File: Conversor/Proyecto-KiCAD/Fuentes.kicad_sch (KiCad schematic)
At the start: 9 parts, among them J7 ConnAlim12-18, U11 LM7805_TO220, U13 THB3-1211, U14 LM1117-3.3

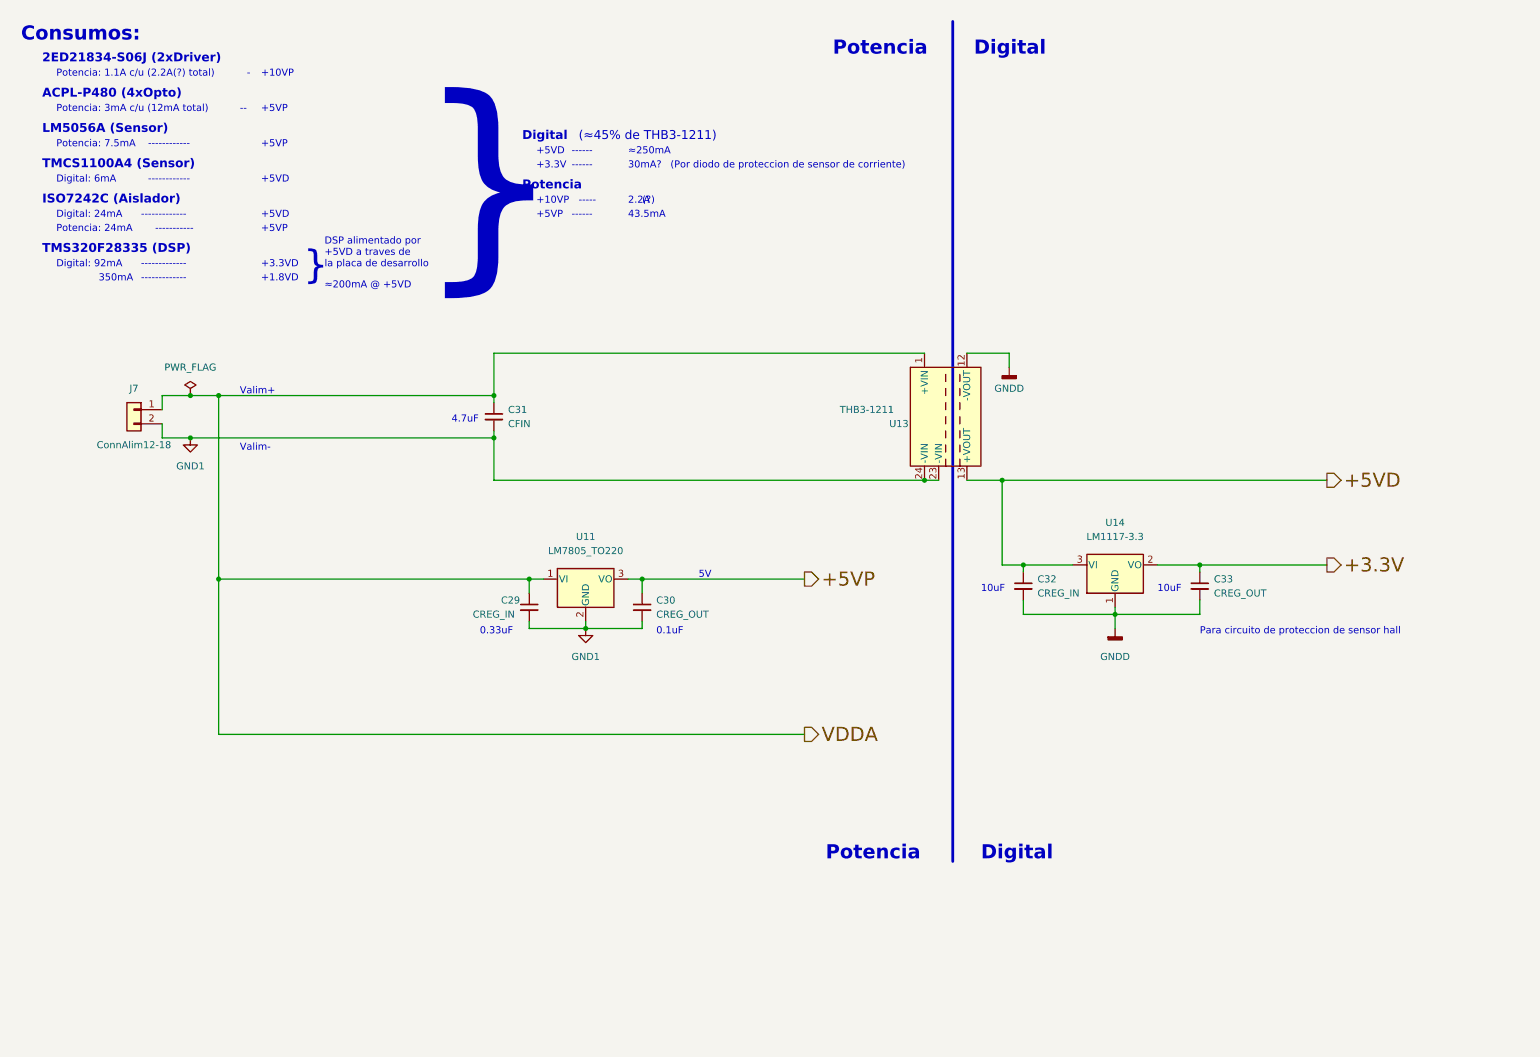
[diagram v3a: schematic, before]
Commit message: Seleccionar componentes de los que me dieron y seguir con la placa adaptadora
- OpAmp OPA365AID para acondicionamiento de señales del sensor de efecto
hall
- Los optos que hay son ACPL-P343 en vez de P480, que necesitan 15-30V
de alimentación. Preguntar si no es mejor cambiarlos por 6N137, de 5V de
Vcc
- Regulador solo hay LM7805 de 5Vout pero también necesito 3.3Vout
- No hay ningún diodo en las cosas que me dieron

Por hacer:
  - Preguntar por los 6N137 y algun regulador de 3V3 out
  - Preguntar por los diodos del puente del conversor
  - Terminar de pasar la placa adaptadora del DSP
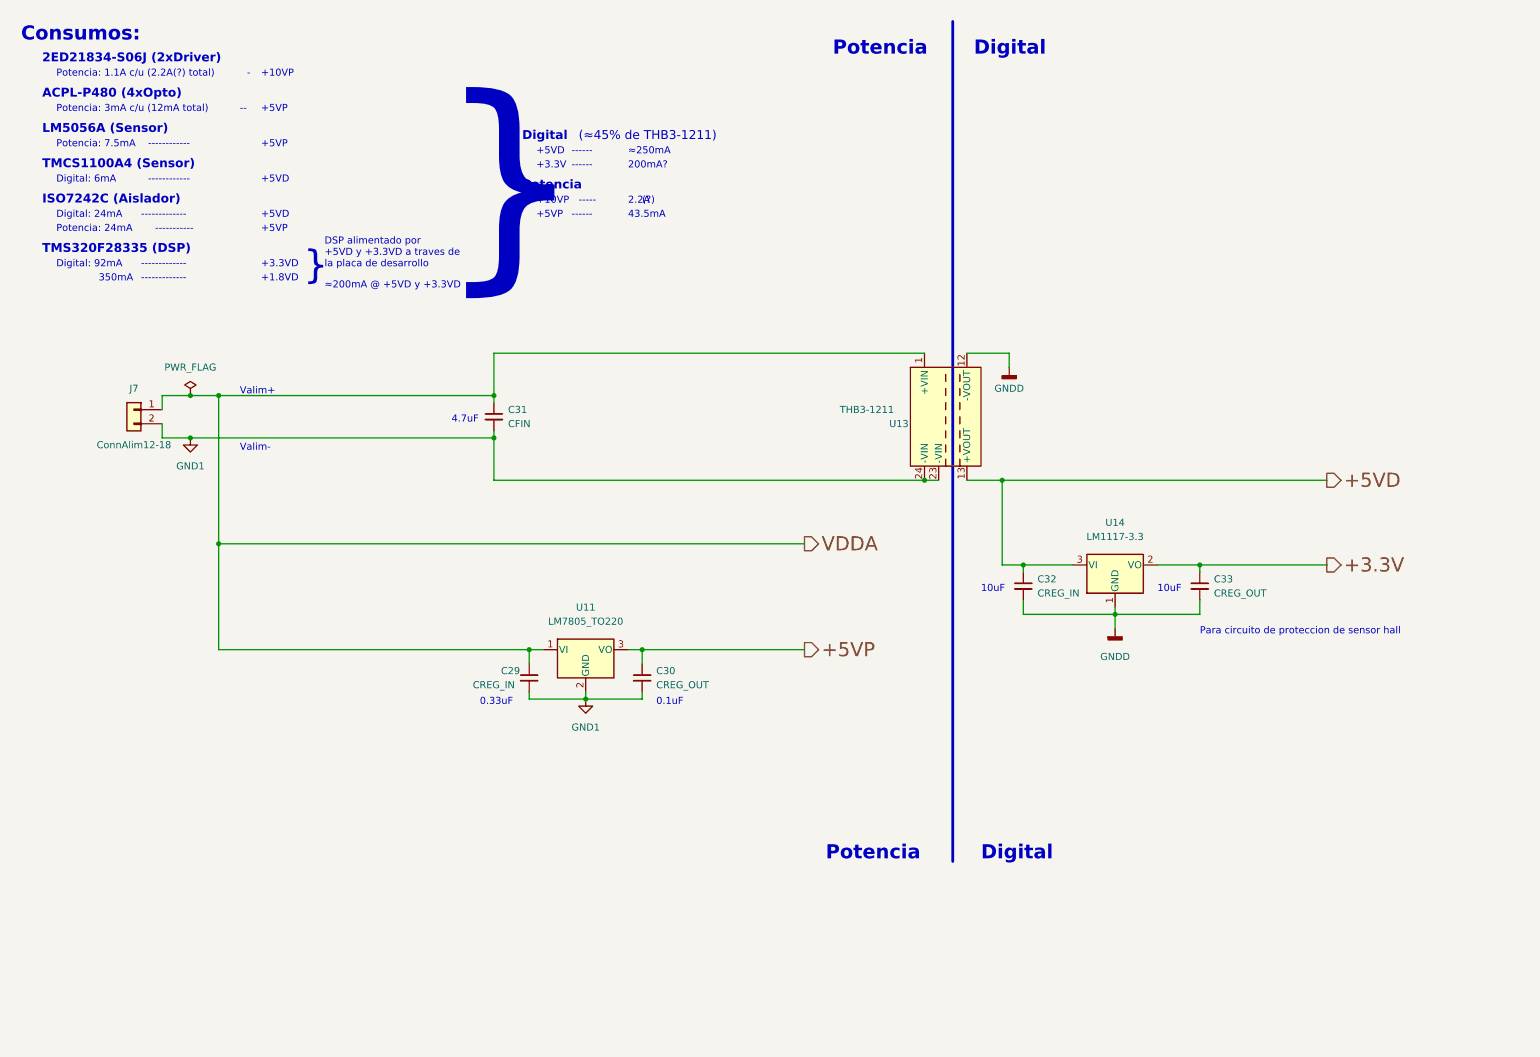
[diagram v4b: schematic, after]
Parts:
- U11: footprint Package_TO_SOT_THT:TO-220-3_Vertical -> Package_TO_SOT_SMD:TO-252-2
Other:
- note added: "200mA?"
- note added: "DSP alimentado por +5VD y +3.3VD a traves de la placa de desarrollo"
- note added: "≈200mA @ +5VD y +3.3VD"
- note removed: "(Por diodo de proteccion de sensor de corriente)"
- note removed: "30mA?"
- note removed: "5V"
- note removed: "DSP alimentado por +5VD a traves de la placa de desarrollo"
- note removed: "≈200mA @ +5VD"
- moved on the sheet: C29, C30, U11

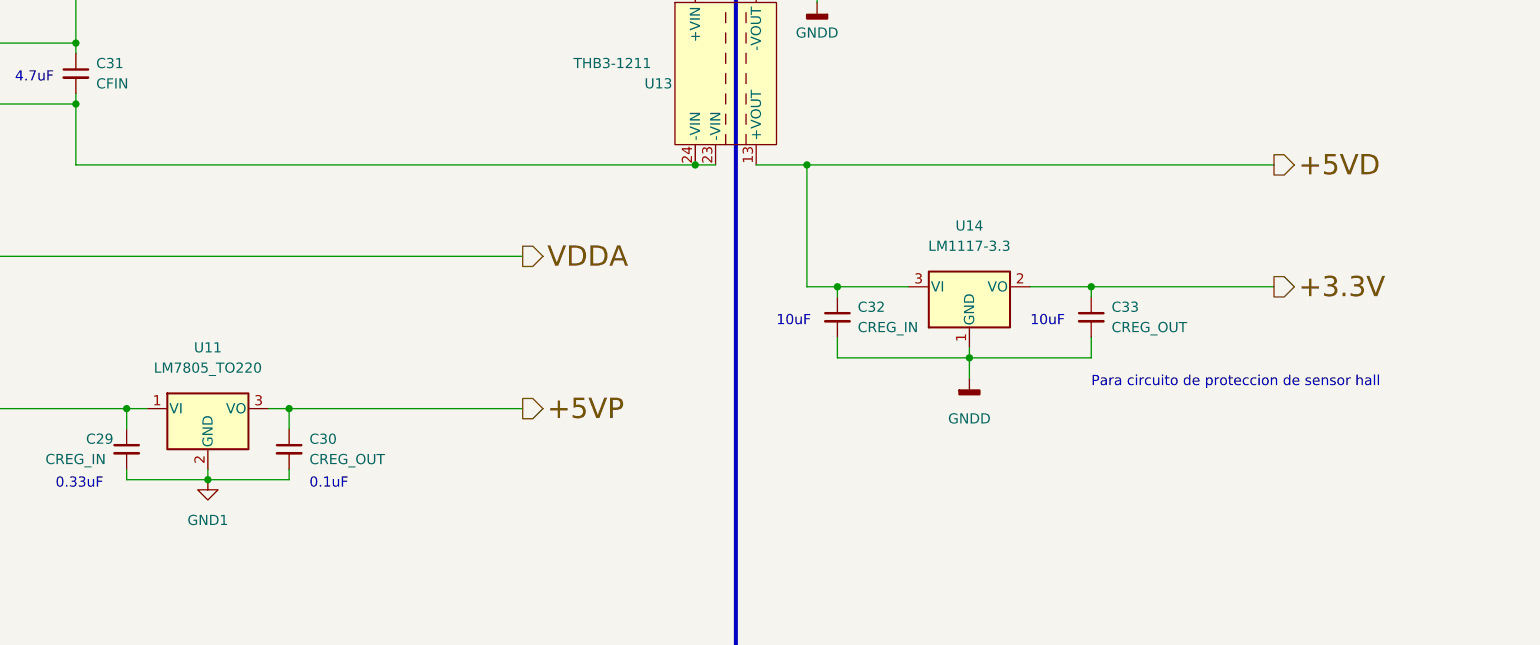
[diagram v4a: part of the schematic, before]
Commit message: Continuar el paso de la placa adaptadora al proyecto
- El bloque de encoder y DAC se eliminan, no son necesarios
- Hay que agregar un selector entre 5V externo y por USB para el DSP, y ver como compatibilizarlo con la alimentación general
- Para el regulador de 3.3V se usa el mismo integrado que en la placa adaptadora (TI LP2985-3.3)
- Los optos son los ACPL-P480 en vez de los P343
Por hacer:
  - Terminar la placa adaptadora (USB-UART, Power Supply e I2C)
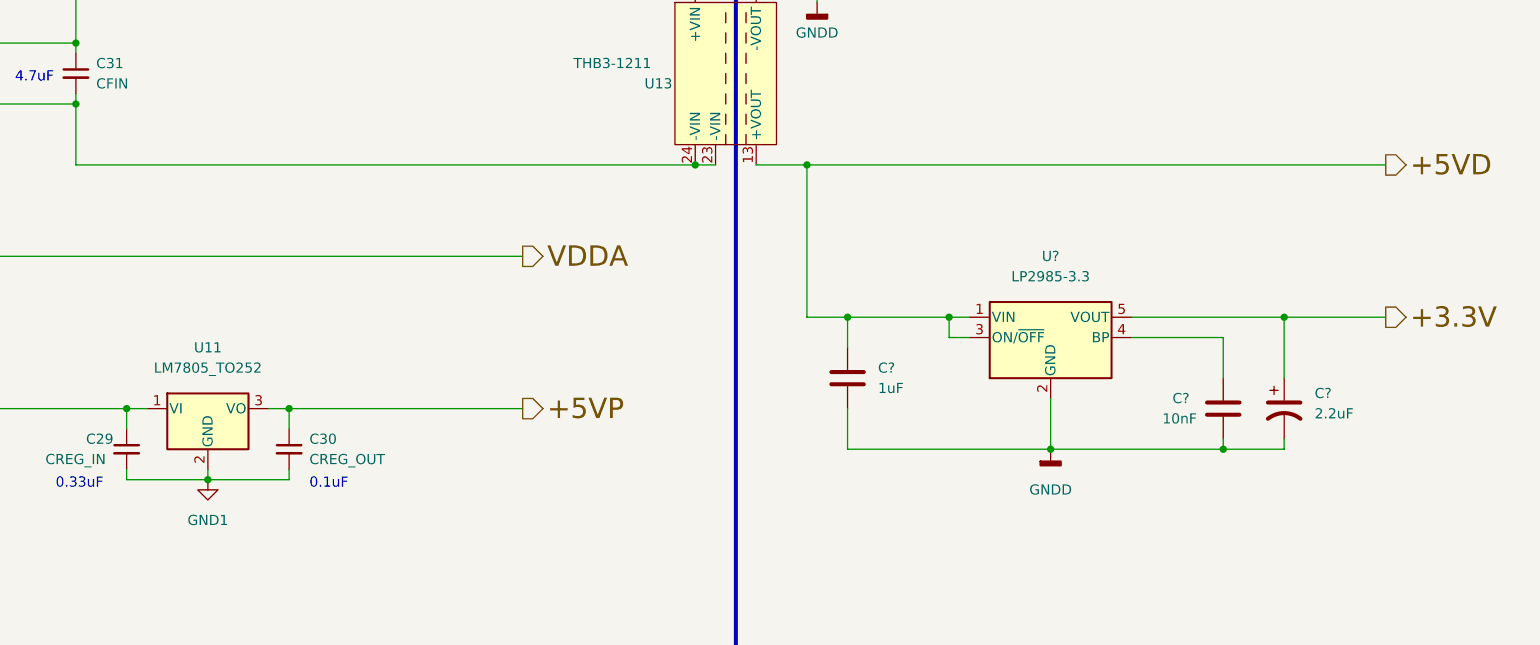
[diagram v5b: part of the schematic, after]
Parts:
- removed C32: CREG_IN, symbol Device:C_Small
- removed C33: CREG_OUT, symbol Device:C_Small
- removed U14: LM1117-3.3, symbol Regulator_Linear:LM1117-3.3
- added C?: 1uF, symbol Device:C
- added C?: 2.2uF, symbol Device:C_Polarized_US
- added C?: 10nF, symbol Device:C
- added U?: LP2985-3.3, Package_TO_SOT_SMD:SOT-23-5, symbol Regulator_Linear:LP2985-3.3
- U11: value LM7805_TO220 -> LM7805_TO252
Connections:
- net +3.3V: now also C?.1, U?.5 (VOUT)
- net +5VD: now also C?.1, U?.1 (VIN), U?.3 (ON/~{OFF})
- net GNDD: now also C?.2, C?.2, C?.2, U?.2 (GND)
- new net: C?.1, U?.4 (BP)
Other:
- note removed: "10uF"
- note removed: "Para circuito de proteccion de sensor hall"

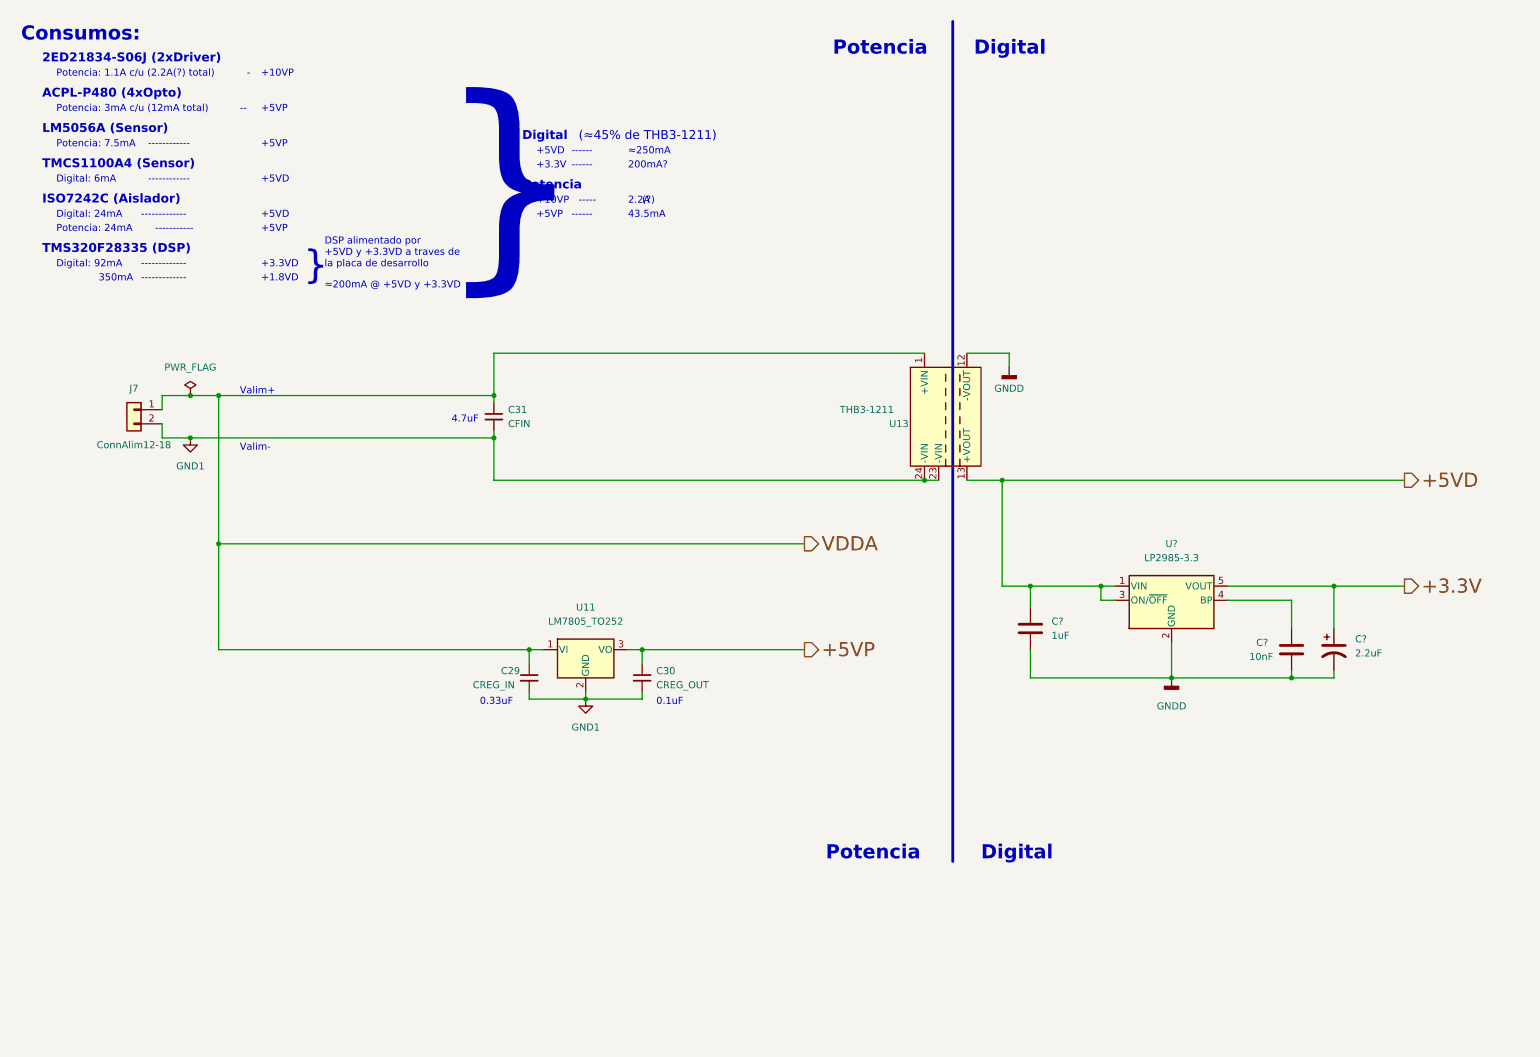
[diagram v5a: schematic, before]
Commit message: Terminar (casi) el traspaso de la placa adaptadora al proyecto
- Queda el selector entre 5V USB y 5V extern, pero todo esta en la hoja
de alimetación general, no dentro de la hoja del DSP
- Cambiar un poco los headers para poder testear (separado en Headers
5V, PWM, ADC, UART, I2C y GPIO)
- Agregar la hoja de datos del LP2985-3.3 (regulador de +3V3)
Por hacer:
  - Ver el tema de la asilacion de las lineas de datos I2C del LM5056,
porque tiene que unirse a una sola linea de datos bidireccional a la
salida del aislador (estan separadas para facilitar la aislación)
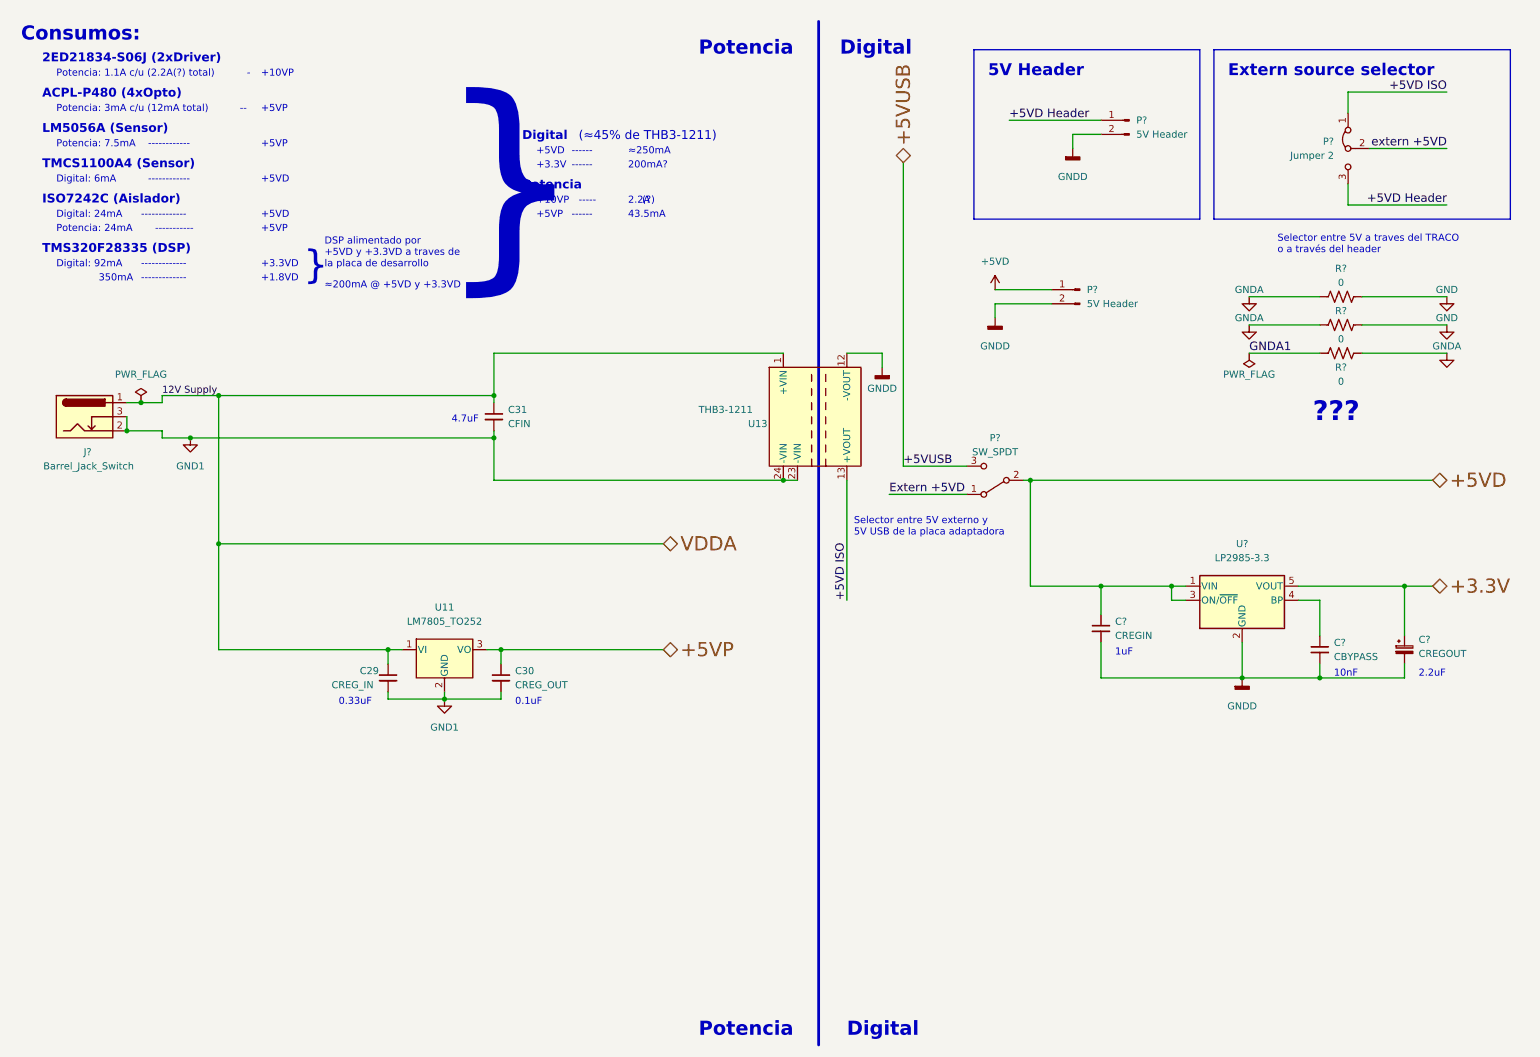
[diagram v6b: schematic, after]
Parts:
- removed C?: 1uF, symbol Device:C
- removed C?: 2.2uF, symbol Device:C_Polarized_US
- removed C?: 10nF, symbol Device:C
- removed J7: ConnAlim12-18, symbol Connector_Generic:Conn_01x02
- added C?: CBYPASS, symbol Device:C_Small
- added C?: CREGOUT, symbol Device:C_Polarized_Small
- added C?: CREGIN, symbol Device:C_Small
- added J?: Barrel_Jack_Switch, Connector_BarrelJack:BarrelJack_GCT_DCJ200-10-A_Horizontal, symbol Connector:Barrel_Jack_Switch
- added P?: SW_SPDT, symbol Switch:SW_SPDT
- added P? (x2): 5V Header, symbol Connector:Conn_01x02_Male
- added P?: Jumper 2, symbol Jumper:Jumper_3_Bridged12
- added R? (x3): 0, symbol Device:R_US
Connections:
- net +3.3V: now also C?.1
- net +5VD: now also C?.1, P?.1 (Pin_1), P?.2 (B); no longer U13.13 (+VOUT)
- net GND1: now also J?.2, J?.3
- net GNDD: now also C?.2, C?.2, C?.2, P?.2 (Pin_2), P?.2 (Pin_2)
- net VDDA: now also J?.1
- net at U?.4 (BP): now also C?.1
- new net +5VD Header: P?.1 (Pin_1), P?.3 (B)
- new net +5VD ISO: P?.1 (A), U13.13 (+VOUT)
- new net +5VUSB: P?.3 (C)
- new net Extern +5VD: P?.1 (A)
- new net GND: R?.1, R?.1, R?.2, R?.2, R?.2
- new net GNDA1: R?.1
- new net extern +5VD: P?.2 (C)
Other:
- note added: "10nF"
- note added: "1uF"
- note added: "2.2uF"
- note added: "5V Header"
- note added: "???"
- note added: "Extern source selector"
- note added: "Selector entre 5V a traves del TRACO o a través del header"
- note added: "Selector entre 5V externo y 5V USB de la placa adaptadora"
- note removed: "Valim+"
- note removed: "Valim-"
- moved on the sheet: C29, C30, U11, U13, U?
